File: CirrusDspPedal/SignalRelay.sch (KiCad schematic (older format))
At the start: 2 parts, among them K1 IM43

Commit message: Completed schematic design
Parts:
- K1: value IM43 -> HFD4/5-S; footprint Relay_SMD:Relay_DPDT_AXICOM_IMSeries_JLeg -> Relay_SMD:Relay_Fujitsu_FTR-B3S
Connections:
- net SignalSwitch renamed RelayCoil_OUT
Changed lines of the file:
@@
 $Descr A4 11693 8268
 encoding utf-8
-Sheet 10 10
+Sheet 7 11
 Title ""
 Date ""
@@
 Comment4 ""
 $EndDescr
+Connection ~ 4650 3200
+Wire Wire Line
+	4300 3200 4650 3200
+Wire Wire Line
+	6225 4775 9225 4775
+Wire Wire Line
+	6225 3950 6225 4775
+Wire Wire Line
+	2750 4775 5825 4775
+Wire Wire Line
+	5825 3950 5825 4775
+Wire Wire Line
+	4650 3200 5325 3200
+Wire Wire Line
+	4650 3500 4650 3200
+Wire Wire Line
+	5325 4100 5325 4300
+Connection ~ 5325 4100
+Wire Wire Line
+	4650 4100 5325 4100
+Wire Wire Line
+	4650 3800 4650 4100
 $Comp
-L Relay:IM43 K1
-U 1 1 5F853388
-P 5725 3650
-F 0 "K1" H 6355 3696 50  0000 L CNN
-F 1 "IM43" H 6355 3605 50  0000 L CNN
-F 2 "Relay_SMD:Relay_DPDT_AXICOM_IMSeries_JLeg" H 5725 3650 50  0001 C CNN
-F 3 "http://www.te.com/commerce/DocumentDelivery/DDEController?Action=srchrtrv&DocNm=108-98001&DocType=SS&DocLang=EN" H 5725 3650 50  0001 C CNN
-	1    5725 3650
-	1    0    0    1
+L Device:D D2
+U 1 1 5F8612FD
+P 4650 3650
+F 0 "D2" V 4600 3875 50  0000 R CNN
+F 1 "1N4148" V 4700 4075 50  0000 R CNN
+F 2 "Diode_SMD:D_SOD-123F" H 4650 3650 50  0001 C CNN
+F 3 "~" H 4650 3650 50  0001 C CNN
+	1    4650 3650
+	0    1    1    0
 $EndComp
+Text HLabel 9225 4775 2    50   Input ~ 0
+FX_OUT
+Text HLabel 2750 4775 0    50   Input ~ 0
+FX_IN
+Text HLabel 9150 2750 2    50   Input ~ 0
+SIGNAL_OUT
 Wire Wire Line
-	5325 3350 5325 3200
+	6125 2750 9150 2750
+Wire Wire Line
+	6125 3350 6125 2750
+Wire Wire Line
+	6025 4150 6025 3950
+Wire Wire Line
+	5625 4150 6025 4150
+Wire Wire Line
+	5625 3950 5625 4150
+Text HLabel 2825 2750 0    50   Input ~ 0
+SIGNAL_IN
+Wire Wire Line
+	5725 2750 2825 2750
+Wire Wire Line
+	5725 3350 5725 2750
+Text HLabel 4300 3200 0    50   Input ~ 0
+RelayCoil_OUT
+Wire Wire Line
+	5325 3950 5325 4100
 $Comp
 L power:GNDS #PWR05
@@
 $EndComp
 Wire Wire Line
-	5325 3950 5325 4100
-Text HLabel 4300 3200 0    50   Input ~ 0
-SignalSwitch
-Wire Wire Line
-	5725 3350 5725 2750
-Wire Wire Line
-	5725 2750 2825 2750
-Text HLabel 2825 2750 0    50   Input ~ 0
-SIGNAL_IN
-Wire Wire Line
-	5625 3950 5625 4150
-Wire Wire Line
-	5625 4150 6025 4150
-Wire Wire Line
-	6025 4150 6025 3950
-Wire Wire Line
-	6125 3350 6125 2750
-Wire Wire Line
-	6125 2750 9150 2750
-Text HLabel 9150 2750 2    50   Input ~ 0
-SIGNAL_OUT
-Text HLabel 2750 4775 0    50   Input ~ 0
-FX_IN
-Text HLabel 9225 4775 2    50   Input ~ 0
-FX_OUT
+	5325 3350 5325 3200
 $Comp
-L Device:D D2
-U 1 1 5F8612FD
-P 4650 3650
-F 0 "D2" V 4600 3875 50  0000 R CNN
-F 1 "1N4148" V 4700 4075 50  0000 R CNN
-F 2 "Diode_SMD:D_SOD-123F" H 4650 3650 50  0001 C CNN
-F 3 "~" H 4650 3650 50  0001 C CNN
-	1    4650 3650
-	0    1    1    0
+L Relay:IM43 K1
+U 1 1 5F853388
+P 5725 3650
+F 0 "K1" H 6525 3575 50  0000 L CNN
+F 1 "HFD4/5-S" H 6475 3675 50  0000 L CNN
+F 2 "Relay_SMD:Relay_Fujitsu_FTR-B3S" H 5725 3650 50  0001 C CNN
+F 3 "https://docs.rs-online.com/9c6f/0900766b81587c84.pdf" H 5725 3650 50  0001 C CNN
+	1    5725 3650
+	1    0    0    1
 $EndComp
-Wire Wire Line
-	4650 3800 4650 4100
-Wire Wire Line
-	4650 4100 5325 4100
-Connection ~ 5325 4100
-Wire Wire Line
-	5325 4100 5325 4300
-Wire Wire Line
-	4650 3500 4650 3200
-Wire Wire Line
-	4650 3200 5325 3200
-Wire Wire Line
-	5825 3950 5825 4775
-Wire Wire Line
-	2750 4775 5825 4775
-Wire Wire Line
-	6225 3950 6225 4775
-Wire Wire Line
-	6225 4775 9225 4775
-Wire Wire Line
-	4300 3200 4650 3200
-Connection ~ 4650 3200
 $EndSCHEMATC

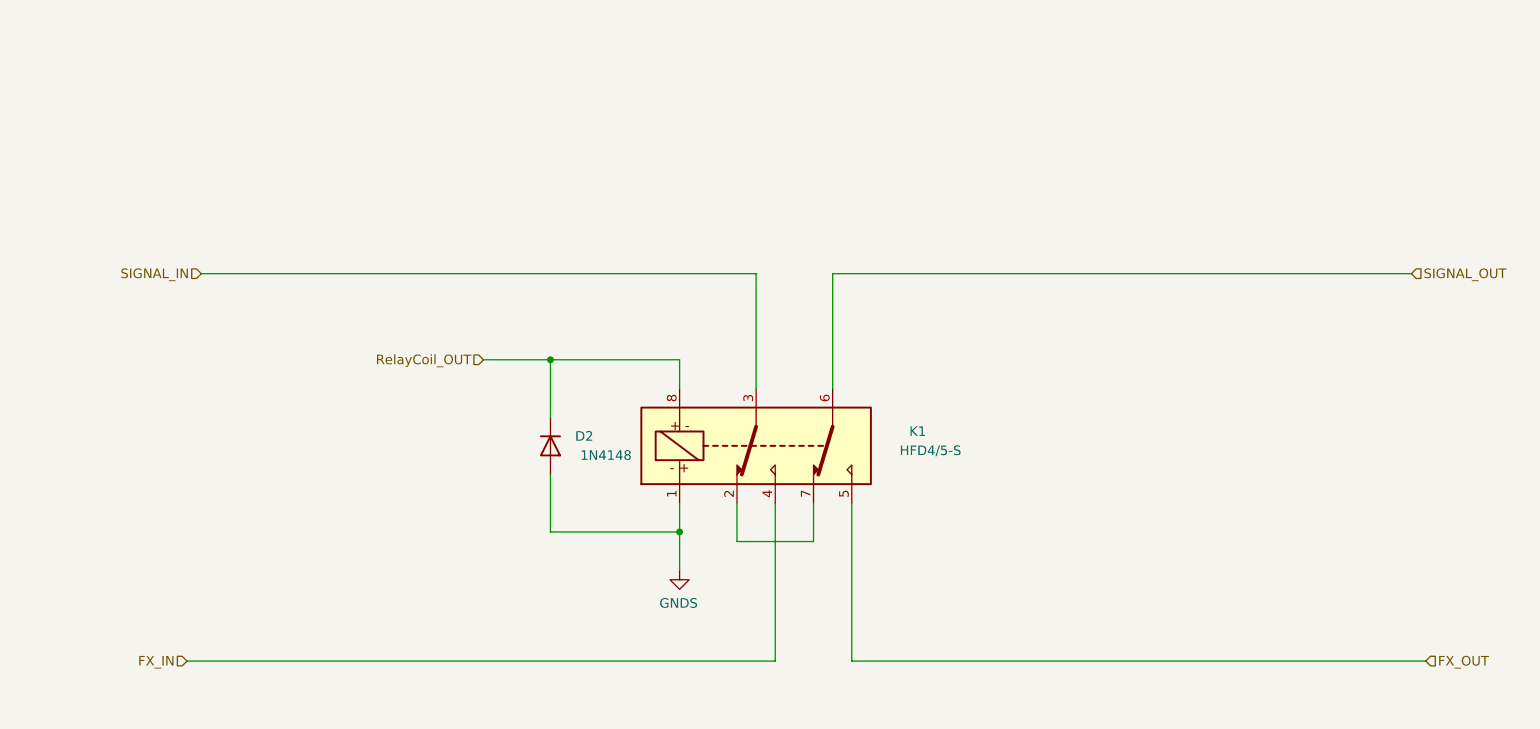
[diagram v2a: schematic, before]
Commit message: Updated design
- Corrected trace going to wrong CS4344 channel output
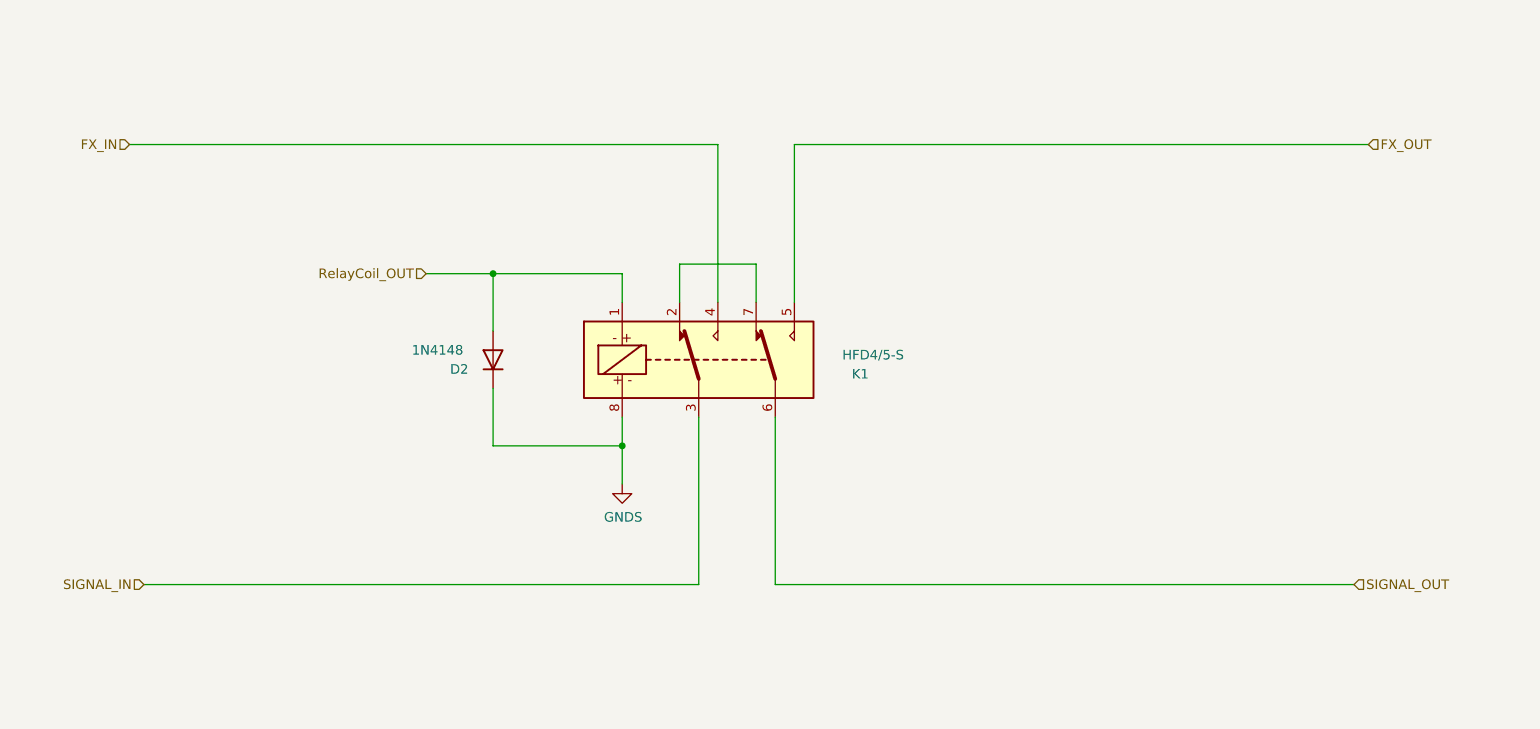
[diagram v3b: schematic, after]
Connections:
- net GNDS: now also D2.1 (K), K1.8; no longer D2.2 (A), K1.1
- net RelayCoil_OUT: now also D2.2 (A), K1.1; no longer D2.1 (K), K1.8
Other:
- moved on the sheet: D2, K1
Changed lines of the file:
@@
 Comment4 ""
 $EndDescr
-Connection ~ 4650 3200
+Connection ~ 4350 2750
 Wire Wire Line
-	4300 3200 4650 3200
+	4000 2750 4350 2750
 Wire Wire Line
-	6225 4775 9225 4775
+	5925 2075 8925 2075
 Wire Wire Line
-	6225 3950 6225 4775
+	5925 2900 5925 2075
 Wire Wire Line
-	2750 4775 5825 4775
+	2450 2075 5525 2075
 Wire Wire Line
-	5825 3950 5825 4775
+	5525 2900 5525 2075
 Wire Wire Line
-	4650 3200 5325 3200
+	4350 2750 5025 2750
 Wire Wire Line
-	4650 3500 4650 3200
+	4350 3050 4350 2750
 Wire Wire Line
-	5325 4100 5325 4300
-Connection ~ 5325 4100
+	5025 3650 5025 3850
 Wire Wire Line
-	4650 4100 5325 4100
+	4350 3650 5025 3650
 Wire Wire Line
-	4650 3800 4650 4100
+	4350 3350 4350 3650
 $Comp
 L Device:D D2
 U 1 1 5F8612FD
-P 4650 3650
-F 0 "D2" V 4600 3875 50  0000 R CNN
-F 1 "1N4148" V 4700 4075 50  0000 R CNN
-F 2 "Diode_SMD:D_SOD-123F" H 4650 3650 50  0001 C CNN
-F 3 "~" H 4650 3650 50  0001 C CNN
-	1    4650 3650
-	0    1    1    0
+P 4350 3200
+F 0 "D2" V 4300 3425 50  0000 R CNN
+F 1 "1N4148" V 4400 3625 50  0000 R CNN
+F 2 "Diode_SMD:D_SOD-123F" H 4350 3200 50  0001 C CNN
+F 3 "~" H 4350 3200 50  0001 C CNN
+	1    4350 3200
+	0    -1   -1   0
 $EndComp
-Text HLabel 9225 4775 2    50   Input ~ 0
+Text HLabel 8925 2075 2    50   Input ~ 0
 FX_OUT
-Text HLabel 2750 4775 0    50   Input ~ 0
+Text HLabel 2450 2075 0    50   Input ~ 0
 FX_IN
-Text HLabel 9150 2750 2    50   Input ~ 0
+Text HLabel 8850 4375 2    50   Input ~ 0
 SIGNAL_OUT
 Wire Wire Line
-	6125 2750 9150 2750
+	5825 4375 8850 4375
 Wire Wire Line
-	6125 3350 6125 2750
+	5825 3500 5825 4375
 Wire Wire Line
-	6025 4150 6025 3950
+	5725 2700 5725 2900
 Wire Wire Line
-	5625 4150 6025 4150
+	5325 2700 5725 2700
 Wire Wire Line
-	5625 3950 5625 4150
-Text HLabel 2825 2750 0    50   Input ~ 0
+	5325 2900 5325 2700
+Text HLabel 2525 4375 0    50   Input ~ 0
 SIGNAL_IN
 Wire Wire Line
-	5725 2750 2825 2750
+	5425 4375 2525 4375
 Wire Wire Line
-	5725 3350 5725 2750
-Text HLabel 4300 3200 0    50   Input ~ 0
+	5425 3500 5425 4375
+Text HLabel 4000 2750 0    50   Input ~ 0
 RelayCoil_OUT
 Wire Wire Line
-	5325 3950 5325 4100
+	5025 2900 5025 2750
 $Comp
 L power:GNDS #PWR05
 U 1 1 5F857915
-P 5325 4300
-F 0 "#PWR05" H 5325 4050 50  0001 C CNN
-F 1 "GNDS" H 5330 4127 50  0000 C CNN
-F 2 "" H 5325 4300 50  0001 C CNN
-F 3 "" H 5325 4300 50  0001 C CNN
-	1    5325 4300
-	-1   0    0    -1
+P 5025 3850
+F 0 "#PWR05" H 5025 3600 50  0001 C CNN
+F 1 "GNDS" H 5030 3677 50  0000 C CNN
+F 2 "" H 5025 3850 50  0001 C CNN
+F 3 "" H 5025 3850 50  0001 C CNN
+	1    5025 3850
+	1    0    0    -1
 $EndComp
 Wire Wire Line
-	5325 3350 5325 3200
+	5025 3500 5025 3650
 $Comp
 L Relay:IM43 K1
 U 1 1 5F853388
-P 5725 3650
-F 0 "K1" H 6525 3575 50  0000 L CNN
-F 1 "HFD4/5-S" H 6475 3675 50  0000 L CNN
-F 2 "Relay_SMD:Relay_Fujitsu_FTR-B3S" H 5725 3650 50  0001 C CNN
-F 3 "https://docs.rs-online.com/9c6f/0900766b81587c84.pdf" H 5725 3650 50  0001 C CNN
-	1    5725 3650
-	1    0    0    1
+P 5425 3200
+F 0 "K1" H 6225 3125 50  0000 L CNN
+F 1 "HFD4/5-S" H 6175 3225 50  0000 L CNN
+F 2 "Relay_SMD:Relay_Fujitsu_FTR-B3S" H 5425 3200 50  0001 C CNN
+F 3 "https://docs.rs-online.com/9c6f/0900766b81587c84.pdf" H 5425 3200 50  0001 C CNN
+	1    5425 3200
+	1    0    0    -1
 $EndComp
+Connection ~ 5025 3650
 $EndSCHEMATC

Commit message: finished revb layout
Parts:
- removed K1: HFD4/5-S, Relay_SMD:Relay_Fujitsu_FTR-B3S, symbol Relay:IM43
- added K1: HFD4/3_S, Relay_SMD:Relay_Fujitsu_FTR-B3S, symbol Relay:IM01
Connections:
- net FX_IN: now also K1.4
- net FX_OUT: now also K1.5
- net GNDS: now also K1.8
- net RelayCoil_OUT: now also K1.1
- net SIGNAL_IN: now also K1.3
- net SIGNAL_OUT: now also K1.6
- new net: K1.2, K1.7
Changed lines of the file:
@@
 Wire Wire Line
 	5025 3500 5025 3650
+Connection ~ 5025 3650
 $Comp
-L Relay:IM43 K1
-U 1 1 5F853388
+L Relay:IM01 K1
+U 1 1 5FA7D624
 P 5425 3200
-F 0 "K1" H 6225 3125 50  0000 L CNN
-F 1 "HFD4/5-S" H 6175 3225 50  0000 L CNN
+F 0 "K1" H 6055 3246 50  0000 L CNN
+F 1 "HFD4/3_S" H 6055 3155 50  0000 L CNN
 F 2 "Relay_SMD:Relay_Fujitsu_FTR-B3S" H 5425 3200 50  0001 C CNN
 F 3 "https://docs.rs-online.com/9c6f/0900766b81587c84.pdf" H 5425 3200 50  0001 C CNN
@@
 	1    0    0    -1
 $EndComp
-Connection ~ 5025 3650
 $EndSCHEMATC

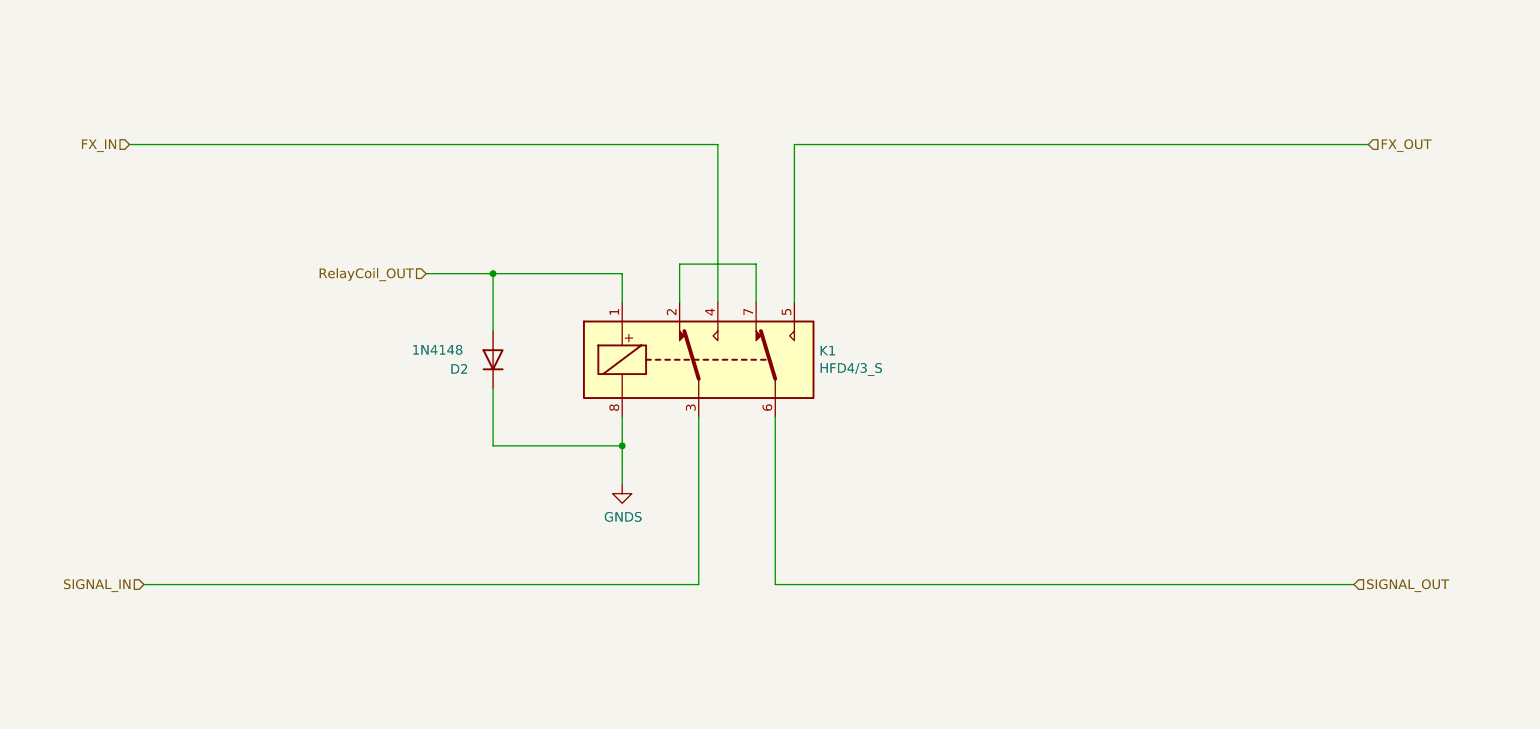
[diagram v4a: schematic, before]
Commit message: updated revb
- Added n-chan and 5V/3V3 jumper for relay
- Moved MCU to the middle of PCB (more space)
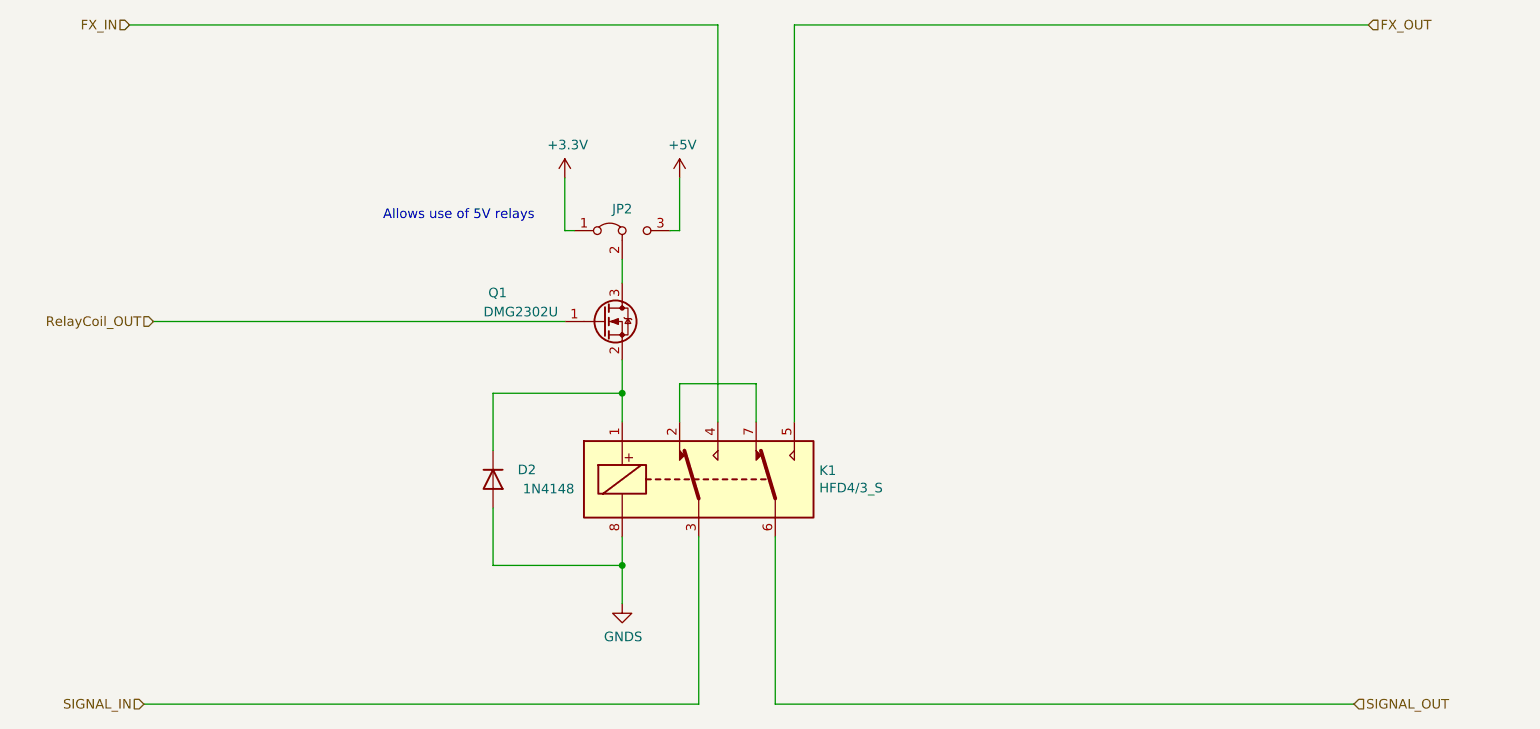
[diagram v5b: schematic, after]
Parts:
- added JP2: Jumper_3_Bridged12, Jumper:SolderJumper-3_P1.3mm_Bridged2Bar12_Pad1.0x1.5mm, symbol Jumper:Jumper_3_Bridged12
- added Q1: DMG2302U, Package_TO_SOT_SMD:SOT-23, symbol Device:Q_NMOS_GSD
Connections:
- net GNDS: now also D2.2 (A); no longer D2.1 (K)
- net RelayCoil_OUT: now also Q1.1 (G); no longer D2.2 (A), K1.1
- new net: D2.1 (K), K1.1, Q1.2 (S)
- new net: JP2.2 (C), Q1.3 (D)
- new net +3V3: JP2.1 (A)
- new net +5V: JP2.3 (B)
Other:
- note added: "Allows use of 5V relays"
- moved on the sheet: D2, K1
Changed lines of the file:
@@
 Comment4 ""
 $EndDescr
-Connection ~ 4350 2750
 Wire Wire Line
-	4000 2750 4350 2750
+	2575 3000 4725 3000
 Wire Wire Line
-	5925 2075 8925 2075
+	5925 1450 8925 1450
 Wire Wire Line
-	5925 2900 5925 2075
+	5925 3525 5925 1450
 Wire Wire Line
-	2450 2075 5525 2075
+	2450 1450 5525 1450
 Wire Wire Line
-	5525 2900 5525 2075
+	5525 3525 5525 1450
 Wire Wire Line
-	4350 2750 5025 2750
+	4350 3675 4350 3375
 Wire Wire Line
-	4350 3050 4350 2750
+	5025 4275 5025 4475
 Wire Wire Line
-	5025 3650 5025 3850
+	4350 4275 5025 4275
 Wire Wire Line
-	4350 3650 5025 3650
-Wire Wire Line
-	4350 3350 4350 3650
+	4350 3975 4350 4275
 $Comp
 L Device:D D2
 U 1 1 5F8612FD
-P 4350 3200
-F 0 "D2" V 4300 3425 50  0000 R CNN
-F 1 "1N4148" V 4400 3625 50  0000 R CNN
-F 2 "Diode_SMD:D_SOD-123F" H 4350 3200 50  0001 C CNN
-F 3 "~" H 4350 3200 50  0001 C CNN
-	1    4350 3200
-	0    -1   -1   0
+P 4350 3825
+F 0 "D2" V 4300 4050 50  0000 R CNN
+F 1 "1N4148" V 4400 4250 50  0000 R CNN
+F 2 "Diode_SMD:D_SOD-123F" H 4350 3825 50  0001 C CNN
+F 3 "~" H 4350 3825 50  0001 C CNN
+	1    4350 3825
+	0    1    1    0
 $EndComp
-Text HLabel 8925 2075 2    50   Input ~ 0
+Text HLabel 8925 1450 2    50   Input ~ 0
 FX_OUT
-Text HLabel 2450 2075 0    50   Input ~ 0
+Text HLabel 2450 1450 0    50   Input ~ 0
 FX_IN
-Text HLabel 8850 4375 2    50   Input ~ 0
+Text HLabel 8850 5000 2    50   Input ~ 0
 SIGNAL_OUT
 Wire Wire Line
-	5825 4375 8850 4375
+	5825 5000 8850 5000
 Wire Wire Line
-	5825 3500 5825 4375
+	5825 4125 5825 5000
 Wire Wire Line
-	5725 2700 5725 2900
+	5725 3325 5725 3525
 Wire Wire Line
-	5325 2700 5725 2700
+	5325 3325 5725 3325
 Wire Wire Line
-	5325 2900 5325 2700
-Text HLabel 2525 4375 0    50   Input ~ 0
+	5325 3525 5325 3325
+Text HLabel 2525 5000 0    50   Input ~ 0
 SIGNAL_IN
 Wire Wire Line
-	5425 4375 2525 4375
+	5425 5000 2525 5000
 Wire Wire Line
-	5425 3500 5425 4375
-Text HLabel 4000 2750 0    50   Input ~ 0
+	5425 4125 5425 5000
+Text HLabel 2575 3000 0    50   Input ~ 0
 RelayCoil_OUT
-Wire Wire Line
-	5025 2900 5025 2750
 $Comp
 L power:GNDS #PWR05
 U 1 1 5F857915
-P 5025 3850
-F 0 "#PWR05" H 5025 3600 50  0001 C CNN
-F 1 "GNDS" H 5030 3677 50  0000 C CNN
-F 2 "" H 5025 3850 50  0001 C CNN
-F 3 "" H 5025 3850 50  0001 C CNN
-	1    5025 3850
+P 5025 4475
+F 0 "#PWR05" H 5025 4225 50  0001 C CNN
+F 1 "GNDS" H 5030 4302 50  0000 C CNN
+F 2 "" H 5025 4475 50  0001 C CNN
+F 3 "" H 5025 4475 50  0001 C CNN
+	1    5025 4475
 	1    0    0    -1
 $EndComp
 Wire Wire Line
-	5025 3500 5025 3650
-Connection ~ 5025 3650
+	5025 4125 5025 4275
+Connection ~ 5025 4275
 $Comp
 L Relay:IM01 K1
 U 1 1 5FA7D624
-P 5425 3200
-F 0 "K1" H 6055 3246 50  0000 L CNN
-F 1 "HFD4/3_S" H 6055 3155 50  0000 L CNN
-F 2 "Relay_SMD:Relay_Fujitsu_FTR-B3S" H 5425 3200 50  0001 C CNN
-F 3 "https://docs.rs-online.com/9c6f/0900766b81587c84.pdf" H 5425 3200 50  0001 C CNN
-	1    5425 3200
+P 5425 3825
+F 0 "K1" H 6055 3871 50  0000 L CNN
+F 1 "HFD4/3_S" H 6055 3780 50  0000 L CNN
+F 2 "Relay_SMD:Relay_Fujitsu_FTR-B3S" H 5425 3825 50  0001 C CNN
+F 3 "https://docs.rs-online.com/9c6f/0900766b81587c84.pdf" H 5425 3825 50  0001 C CNN
+	1    5425 3825
 	1    0    0    -1
 $EndComp
+$Comp
+L Device:Q_NMOS_GSD Q1
+U 1 1 5FAC2041
+P 4925 3000
+F 0 "Q1" H 4325 3150 50  0000 L CNN
+F 1 "DMG2302U" H 4300 3050 50  0000 L CNN
+F 2 "Package_TO_SOT_SMD:SOT-23" H 5125 3100 50  0001 C CNN
+F 3 "https://www.mouser.co.uk/datasheet/2/115/DMG2302U-1512446.pdf" H 4925 3000 50  0001 C CNN
+	1    4925 3000
+	1    0    0    -1
+$EndComp
+Wire Wire Line
+	5025 3200 5025 3375
+Wire Wire Line
+	4350 3375 5025 3375
+Connection ~ 5025 3375
+Wire Wire Line
+	5025 3375 5025 3525
+$Comp
+L power:+5V #PWR024
+U 1 1 5FAD30B5
+P 5325 2250
+F 0 "#PWR024" H 5325 2100 50  0001 C CNN
+F 1 "+5V" H 5340 2423 50  0000 C CNN
+F 2 "" H 5325 2250 50  0001 C CNN
+F 3 "" H 5325 2250 50  0001 C CNN
+	1    5325 2250
+	1    0    0    -1
+$EndComp
+$Comp
+L power:+3.3V #PWR023
+U 1 1 5FAD37AF
+P 4725 2250
+F 0 "#PWR023" H 4725 2100 50  0001 C CNN
+F 1 "+3.3V" H 4740 2423 50  0000 C CNN
+F 2 "" H 4725 2250 50  0001 C CNN
+F 3 "" H 4725 2250 50  0001 C CNN
+	1    4725 2250
+	1    0    0    -1
+$EndComp
+Wire Wire Line
+	5275 2525 5325 2525
+Wire Wire Line
+	5325 2525 5325 2250
+Wire Wire Line
+	4775 2525 4725 2525
+Wire Wire Line
+	4725 2525 4725 2250
+$Comp
+L Jumper:Jumper_3_Bridged12 JP2
+U 1 1 5FAE6E12
+P 5025 2525
+F 0 "JP2" H 5025 2638 50  0000 C CNN
+F 1 "Jumper_3_Bridged12" H 5025 2638 50  0001 C CNN
+F 2 "Jumper:SolderJumper-3_P1.3mm_Bridged2Bar12_Pad1.0x1.5mm" H 5025 2525 50  0001 C CNN
+F 3 "~" H 5025 2525 50  0001 C CNN
+	1    5025 2525
+	1    0    0    -1
+$EndComp
+Wire Wire Line
+	5025 2675 5025 2800
+Text Notes 3775 2475 0    50   ~ 0
+Allows use of 5V relays
 $EndSCHEMATC
